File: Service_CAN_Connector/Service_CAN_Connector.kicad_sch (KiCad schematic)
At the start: 29 parts, among them J1 CAN1, J10 Shield, J11 Shield, J12 Shield, J13 CAN Power, J14 CAN1_Terminator, J15 CAN1_Terminator, J16 CAN1_Terminator, J17 CAN1_Terminator, J18 CAN1_Terminator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

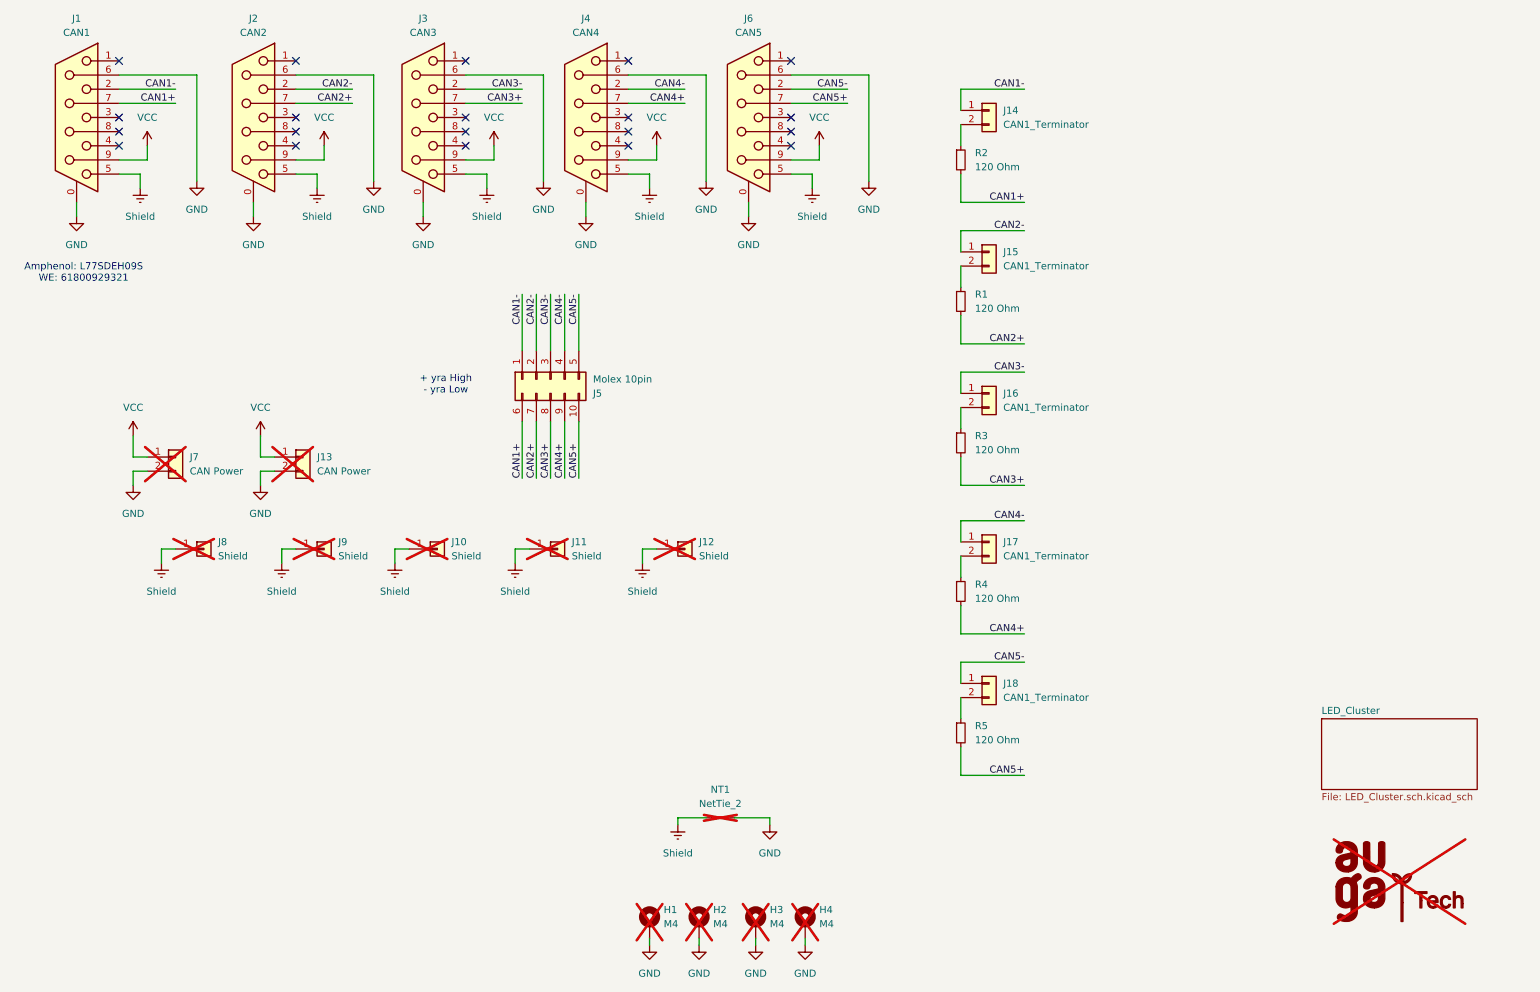
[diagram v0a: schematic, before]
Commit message: Service can connector Rev B
Also added molex 10 pin connector 3d model
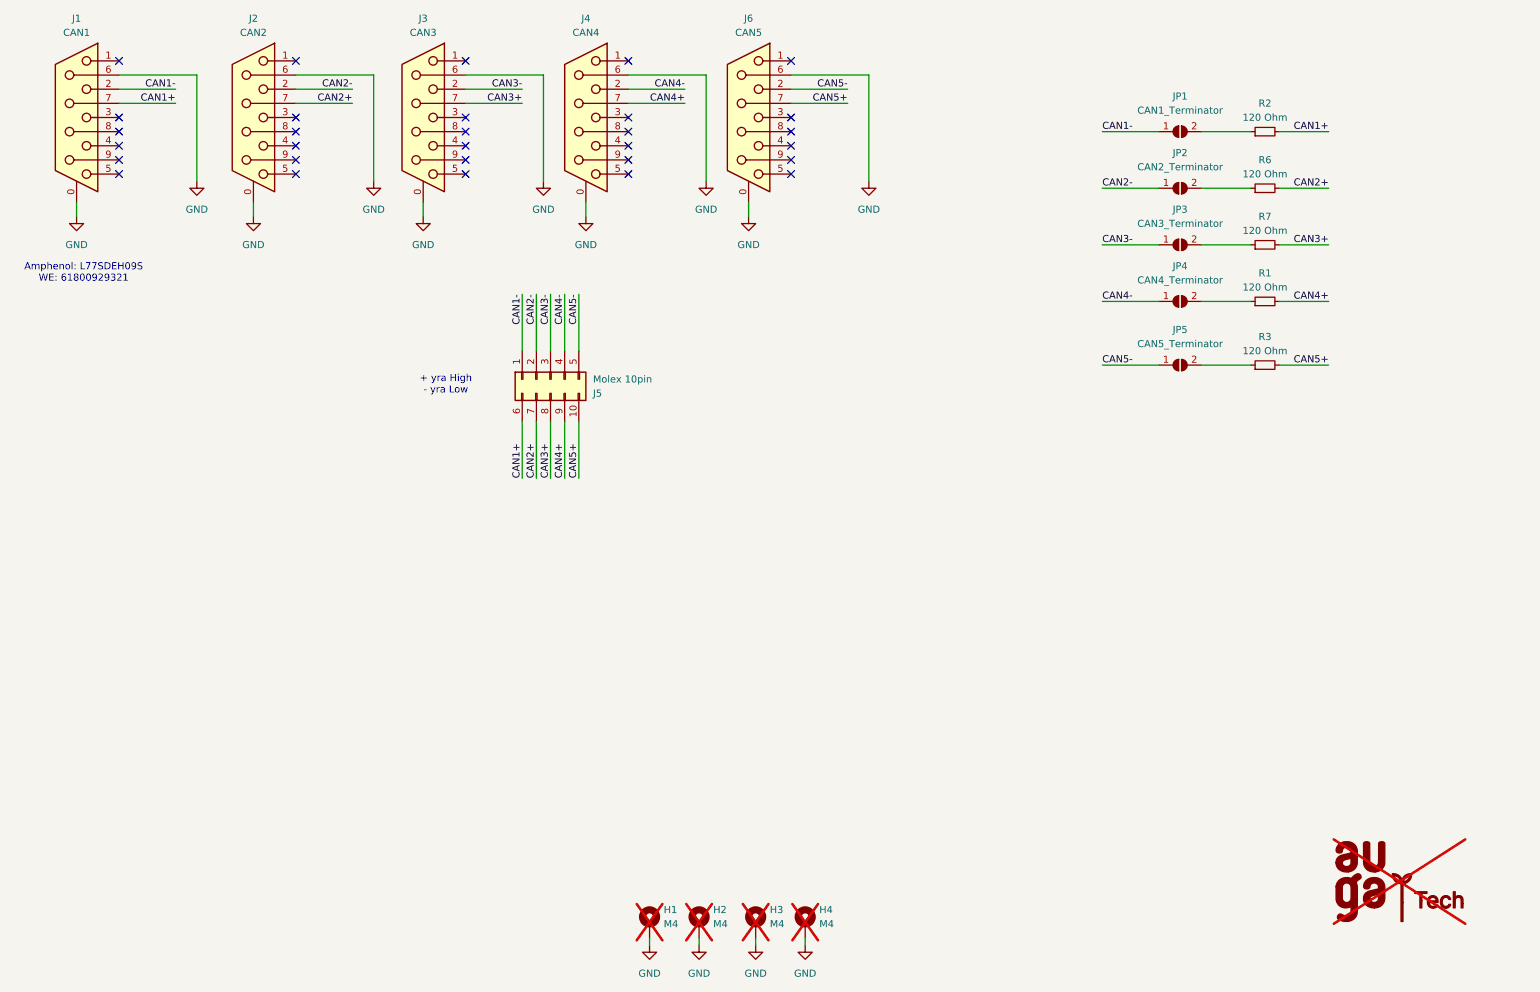
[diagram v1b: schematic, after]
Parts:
- removed J10, J11, J12, J8, J9: Shield, Connector_PinHeader_2.54mm:PinHeader_1x01_P2.54mm_Vertical, symbol Connector_Generic:Conn_01x01
- removed J13, J7: CAN Power, Connector_Molex:Molex_Mini-Fit_Jr_5566-02A_2x01_P4.20mm_Vertical, symbol Connector_Generic:Conn_01x02
- removed J14, J15, J16, J17, J18: CAN1_Terminator, Connector_PinHeader_2.54mm:PinHeader_1x02_P2.54mm_Vertical, symbol Connector_Generic:Conn_01x02
- removed NT1: NetTie_2, NetTie:NetTie-2_THT_Pad0.3mm, symbol Device:NetTie_2
- removed R4, R5: 120 Ohm, Resistor_SMD:R_0805_2012Metric, symbol Device:R_Small
- added JP1: CAN1_Terminator, Jumper:SolderJumper-2_P1.3mm_Open_RoundedPad1.0x1.5mm, symbol Jumper:SolderJumper_2_Open
- added JP2: CAN2_Terminator, Jumper:SolderJumper-2_P1.3mm_Open_RoundedPad1.0x1.5mm, symbol Jumper:SolderJumper_2_Open
- added JP3: CAN3_Terminator, Jumper:SolderJumper-2_P1.3mm_Open_RoundedPad1.0x1.5mm, symbol Jumper:SolderJumper_2_Open
- added JP4: CAN4_Terminator, Jumper:SolderJumper-2_P1.3mm_Open_RoundedPad1.0x1.5mm, symbol Jumper:SolderJumper_2_Open
- added JP5: CAN5_Terminator, Jumper:SolderJumper-2_P1.3mm_Open_RoundedPad1.0x1.5mm, symbol Jumper:SolderJumper_2_Open
- added R6, R7: 120 Ohm, Resistor_SMD:R_0805_2012Metric, symbol Device:R_Small
- J5: footprint Connector_Molex:Molex_Mini-Fit_Jr_5569-10A1_2x05_P4.20mm_Horizontal -> Connector_Molex:Molex_Mini-Fit_Jr_5566-10A2_2x05_P4.20mm_Vertical; JLCPCB Part # C505176 -> (none); MFR_PN (none) -> 39299103
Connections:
- net CAN1-: now also JP1.1 (A)
- net CAN2+: now also R6.2; no longer R1.2
- net CAN2-: now also JP2.1 (A)
- net CAN3+: now also R7.2; no longer R3.2
- net CAN3-: now also JP3.1 (A)
- net CAN4+: now also R1.2
- net CAN4-: now also JP4.1 (A)
- net CAN5+: now also R3.2
- net CAN5-: now also JP5.1 (A)
- net at R3.1: now also JP5.2 (B)
- net at R1.1: now also JP4.2 (B)
- net at R2.1: now also JP1.2 (B)
- removed net Shield: J1.5, J2.5, J3.5, J4.5, J6.5
- removed net VCC: J1.9, J2.9, J3.9, J4.9, J6.9
- new net: JP2.2 (B), R6.1
- new net: JP3.2 (B), R7.1
- no-connect marks 20 -> 30
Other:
- removed sheet LED_Cluster
- moved on the sheet: R2
